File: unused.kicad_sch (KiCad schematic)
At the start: 38 parts, among them U12 MAX8556ETE, U13 MAX8556ETE, U14 MAX8556ETE, U15 TPS74201RGWR, U16 TPS74201RGWR

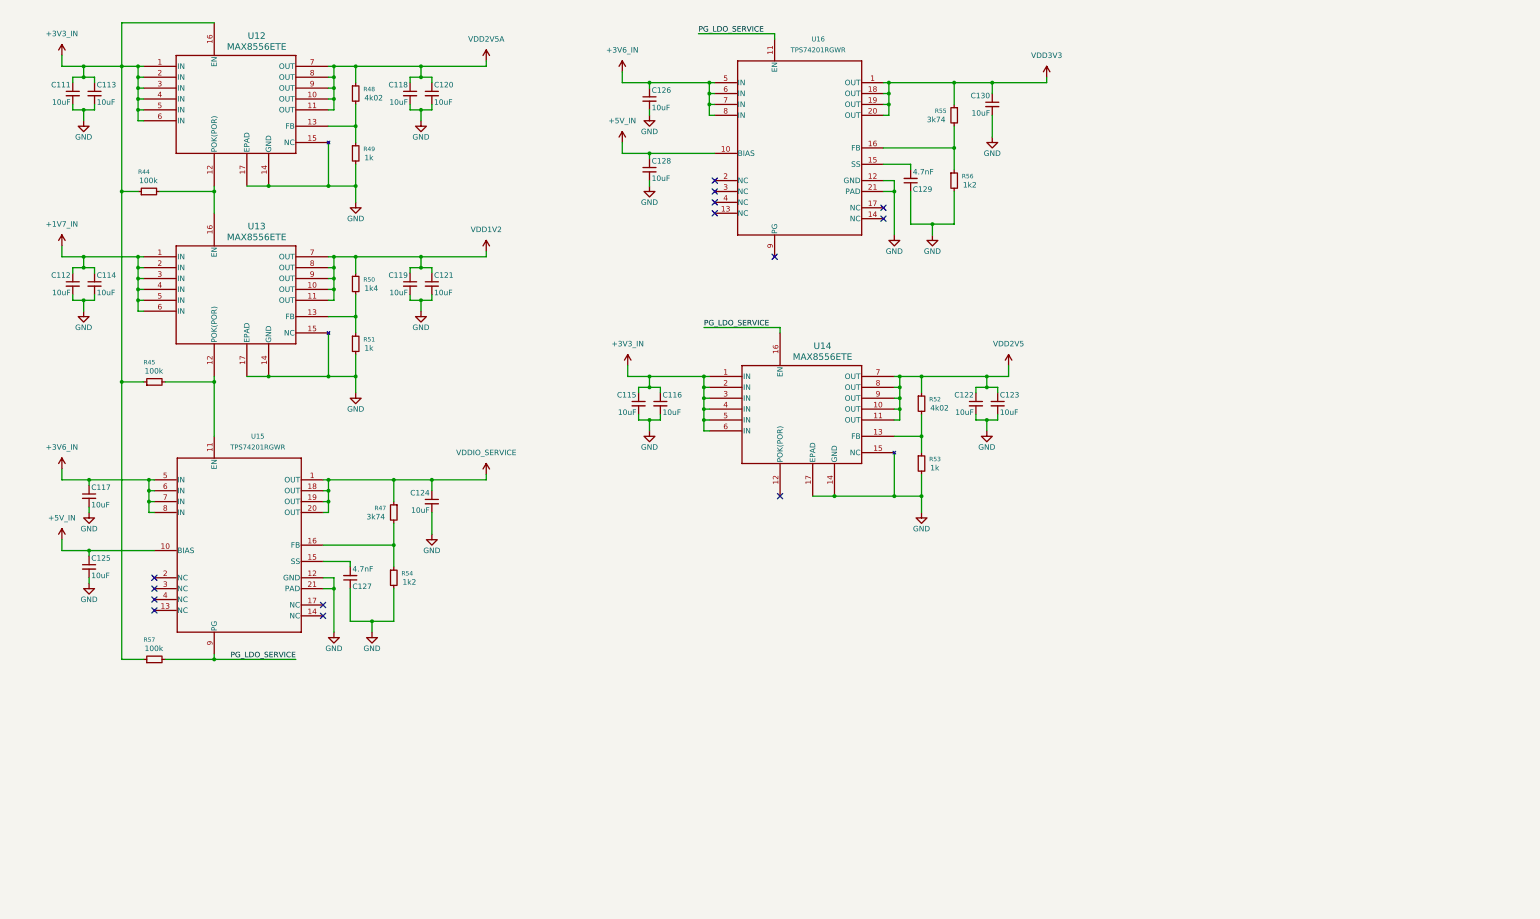
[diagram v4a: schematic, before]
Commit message: finished PCB
finished power tree and power planes. Completed silkscreen placement. Added test points
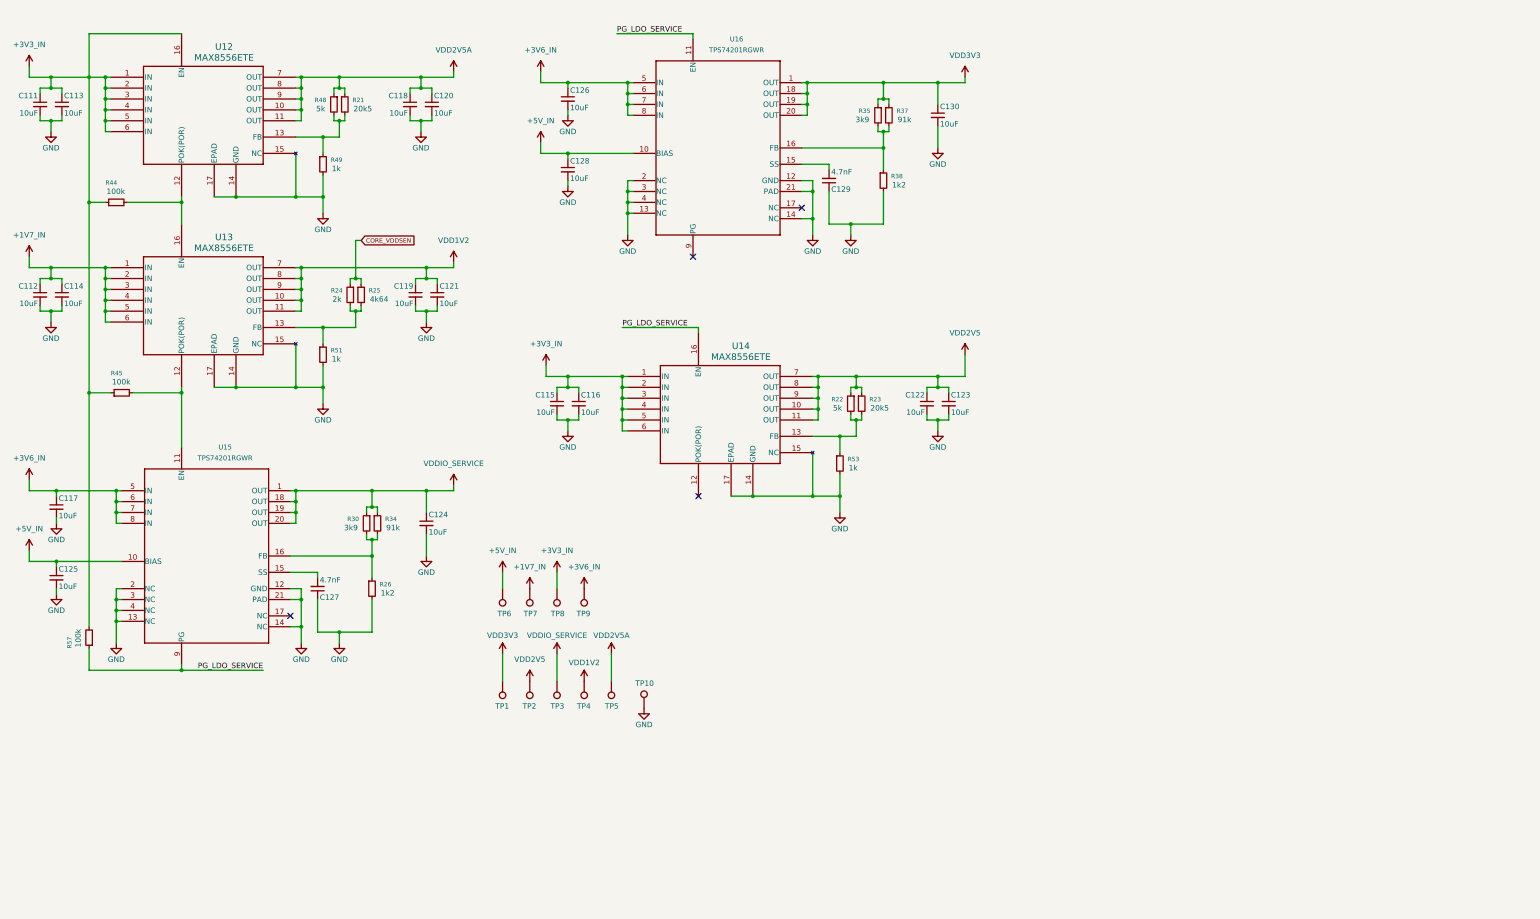
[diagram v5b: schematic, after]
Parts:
- removed R47, R55: 3k74, Resistor_SMD:R_0402_1005Metric_Pad0.72x0.64mm_HandSolder, symbol Device:R_Small
- removed R50: 1k4, Resistor_SMD:R_0402_1005Metric_Pad0.72x0.64mm_HandSolder, symbol Device:R_Small
- removed R52: 4k02, Resistor_SMD:R_0402_1005Metric_Pad0.72x0.64mm_HandSolder, symbol Device:R_Small
- removed R54, R56: 1k2, Resistor_SMD:R_0402_1005Metric_Pad0.72x0.64mm_HandSolder, symbol Device:R_Small
- added R21, R23: 20k5, Resistor_SMD:R_0402_1005Metric_Pad0.72x0.64mm_HandSolder, symbol Device:R_Small
- added R22: 5k, Resistor_SMD:R_0402_1005Metric_Pad0.72x0.64mm_HandSolder, symbol Device:R_Small
- added R24: 2k, Resistor_SMD:R_0402_1005Metric_Pad0.72x0.64mm_HandSolder, symbol Device:R_Small
- added R25: 4k64, Resistor_SMD:R_0402_1005Metric_Pad0.72x0.64mm_HandSolder, symbol Device:R_Small
- added R26, R38: 1k2, Resistor_SMD:R_0402_1005Metric_Pad0.72x0.64mm_HandSolder, symbol Device:R_Small
- added R30, R35: 3k9, Resistor_SMD:R_0402_1005Metric_Pad0.72x0.64mm_HandSolder, symbol Device:R_Small
- added R34, R37: 91k, Resistor_SMD:R_0402_1005Metric_Pad0.72x0.64mm_HandSolder, symbol Device:R_Small
- added TP1, TP10, TP2, TP3, TP4, TP5: TestPoint, DataHub_Footprints:Test_Point, symbol Connector:TestPoint
- added TP6, TP7, TP8, TP9: TestPoint, DataHub_Footprints:PTH_pad_2x0.8, symbol Connector:TestPoint
- C127, C129: footprint Capacitor_SMD:C_0603_1608Metric_Pad1.08x0.95mm_HandSolder -> Capacitor_SMD:C_0402_1005Metric_Pad0.74x0.62mm_HandSolder
- R48: value 4k02 -> 5k
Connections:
- net +1V7_IN: now also TP7.1
- net +3V3_IN: now also R57.2, TP8.1; no longer R57.1
- net +3V6_IN: now also TP9.1
- net +5V_IN: now also TP6.1
- net GND: now also U15.13 (NC), U15.14 (NC), U15.2 (NC), U15.3 (NC), U15.4 (NC), U16.13 (NC), U16.14 (NC), U16.2 (NC), U16.3 (NC), U16.4 (NC), R26.2, R38.2, TP10.1
- net PG_LDO_SERVICE: now also R57.1; no longer R57.2
- net VDD1V2: now also TP4.1
- net VDD2V5: now also R22.1, R23.1, TP2.1
- net VDD2V5A: now also R21.1, TP5.1
- net VDD3V3: now also R35.1, R37.1, TP1.1
- net VDDIO_SERVICE: now also R30.1, R34.1, TP3.1
- net at R53.1, U14.13 (FB): now also R22.2, R23.2
- net at U16.16 (FB): now also R35.2, R37.2, R38.1
- net at R51.1, U13.13 (FB): now also R24.2, R25.2
- net at R48.2, R49.1, U12.13 (FB): now also R21.2
- net at U15.16 (FB): now also R26.1, R30.2, R34.2
- new net CORE_VDDSEN: R24.1, R25.1
- no-connect marks 14 -> 4
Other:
- moved on the sheet: C111, C112, C113, C114, C115, C116, C117, C118, C119, C120, C121, C122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

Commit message: pre-order adjustments
DF9 connectors footprint adjusted.
Dimensions of board edges changed.
Placement of DF9 adjusted.
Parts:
- renumbered C117 to C100, C125 to C101, C113 to C102, C114 to C103, C127 to C104, C118 to C105, C119 to C106, C124 to C107, C120 to C108, C121 to C109, C115 to C110, C126 to C111, C128 to C112, C116 to C113, C129 to C114, C122 to C115, C130 to C116, C123 to C117, C111 to C98, C112 to C99, R57 to R19, R44 to R20, R45 to R21, R49 to R27, R51 to R28, R48 to R29, R21 to R30, R24 to R31, R25 to R32, R30 to R33, R26 to R34, R34 to R36, R53 to R37, R22 to R38, R23 to R39, R35 to R40, R38 to R41, R37 to R42, TP6 to TP1, TP1 to TP2, TP7 to TP3, TP2 to TP4, TP8 to TP5, TP3 to TP6, TP9 to TP7, TP4 to TP8, TP5 to TP9, U15 to U10, U14 to U12, U16 to U13, U12 to U8, U13 to U9
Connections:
- net GND: no longer U8.15 (NC)
- no-connect marks 4 -> 5

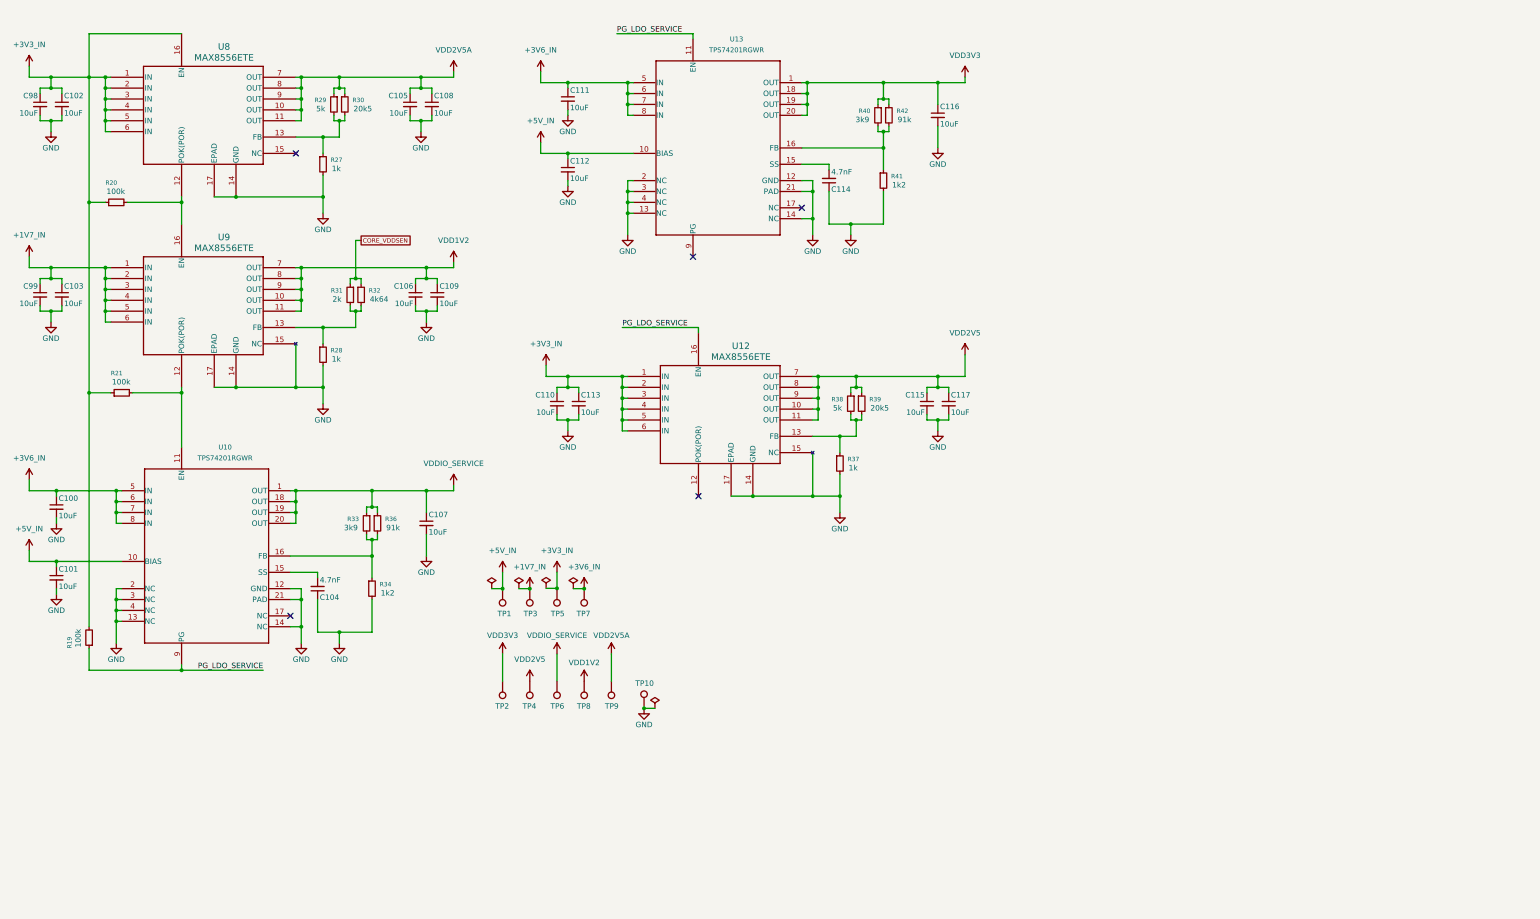
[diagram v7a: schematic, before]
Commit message: pre order adjustments. Board symmetry
adjusted little things brought up by DFM checker of JLCPCB. Board's edges fully symmetrical on y axis. 2mm shift on x axis of the DF9s maintained
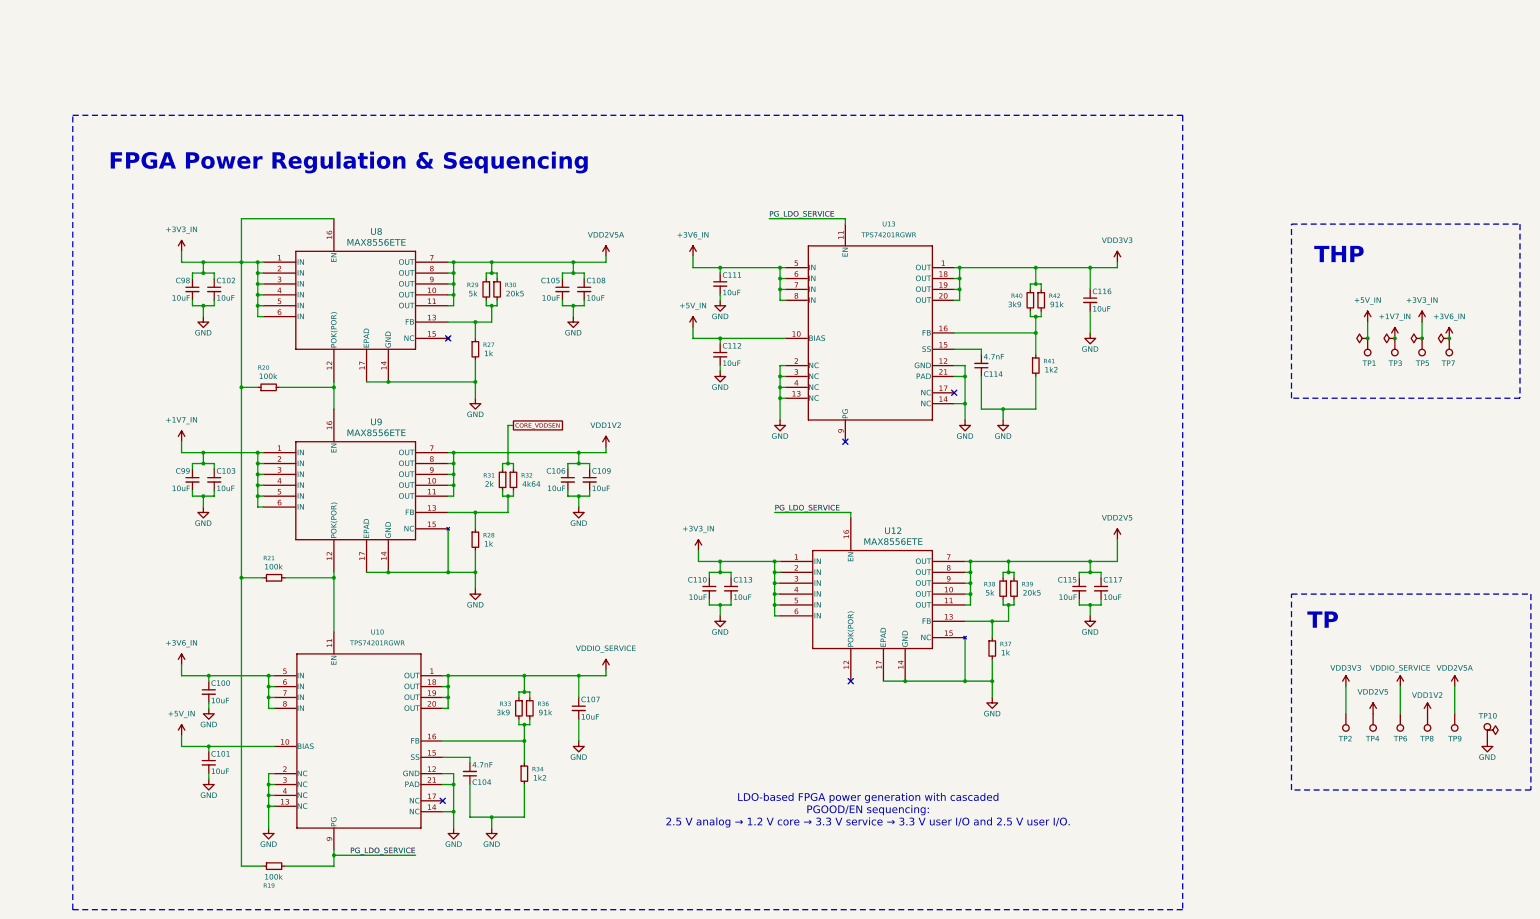
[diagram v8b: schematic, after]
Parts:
- TP1: value TestPoint -> 5V
- TP10: value TestPoint -> GND
- TP2, TP5, TP6: value TestPoint -> 3V3
- TP3: value TestPoint -> 1V7
- TP4: value TestPoint -> 2V5
- TP7: value TestPoint -> 3V6
- TP8: value TestPoint -> 1V2
- TP9: value TestPoint -> 2V5A
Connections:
- net +3V3_IN: now also R19.1; no longer R19.2
- net PG_LDO_SERVICE: now also R19.2; no longer R19.1
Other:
- note added: "FPGA Power Regulation & Sequencing"
- note added: "LDO-based FPGA power generation with cascaded PGOOD/EN sequencing: 2.5 V analog → 1.2 V core → 3.3 V service → 3.3 V user I/O and 2.5 V user I/O."
- note added: "THP"
- note added: "TP"
- moved on the sheet: C100, C101, C102, C103, C104, C105, C106, C107, C108, C109, C110, C111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
